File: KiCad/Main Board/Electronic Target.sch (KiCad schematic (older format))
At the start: 71 parts, among them J1 BHR-12-UVA, J10 EBWA-04-B, J11 640456-6, J12 0475890001, J9 Header 4x2, Q1 DWN1019UVT-7, Q2 DMN1019UVT-7, U1 PDSE1-S5-D6-M-TR, U2 LM339, U3 74HC74, U4 74LV8154, U5 74HC74, U6 74HC00, U7 74LV8154, U8 FT230XS-U, U9 LM75AIMX_NOPB, X1 8M0

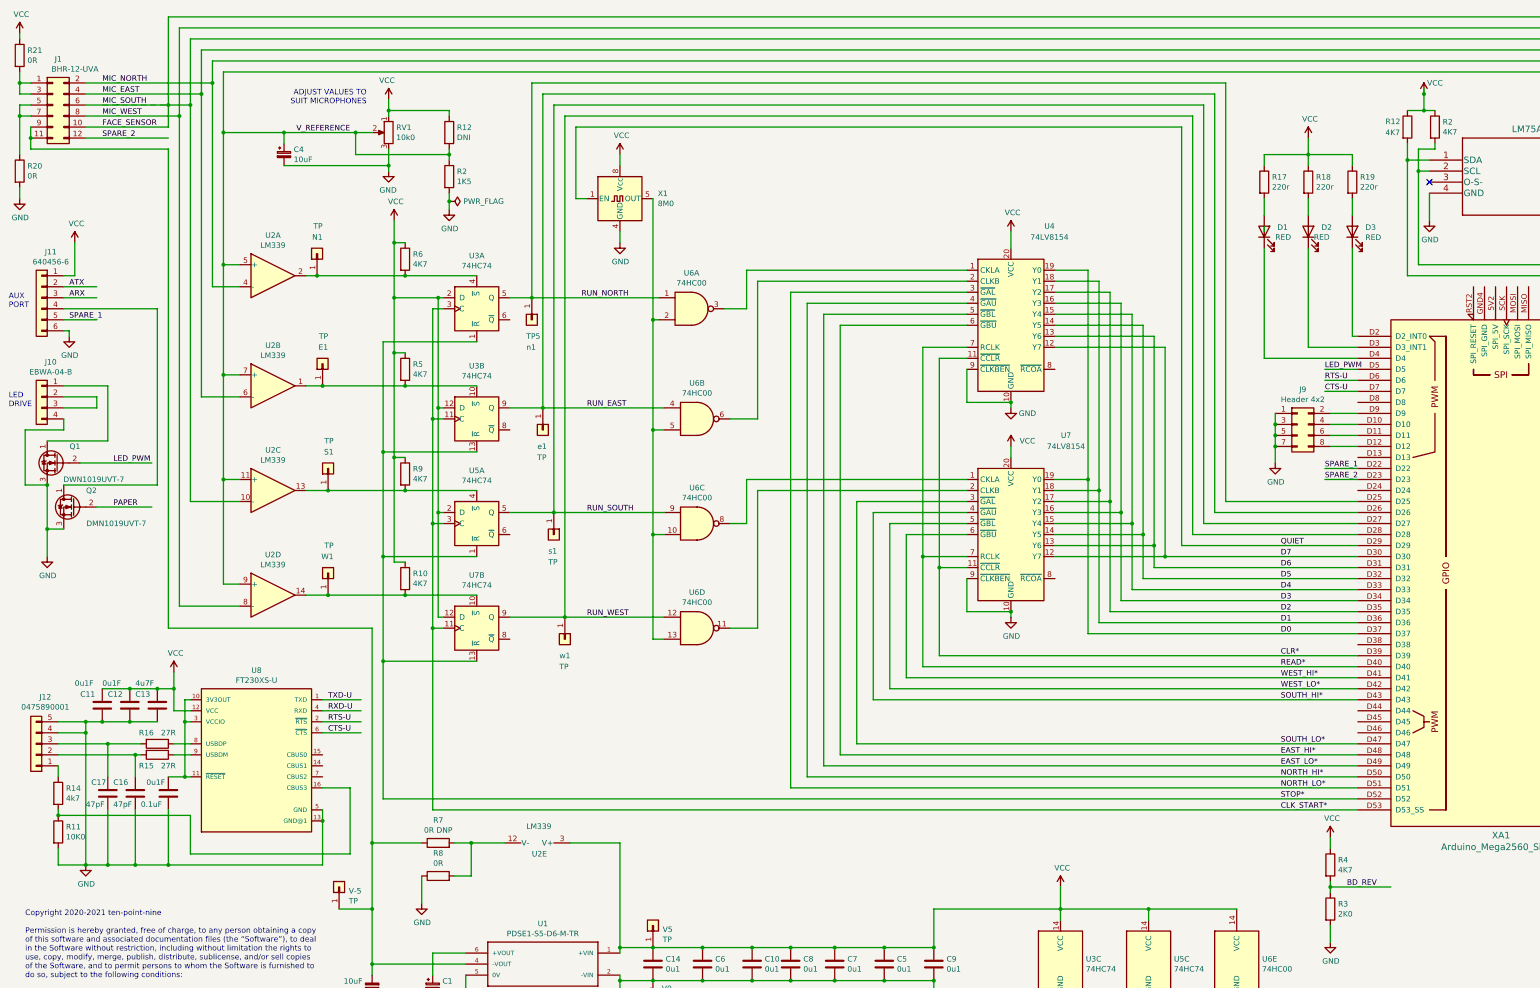
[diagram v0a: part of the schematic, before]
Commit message: Corrected errors in Schematic
Found a resistor error and reannotated the main board schematic
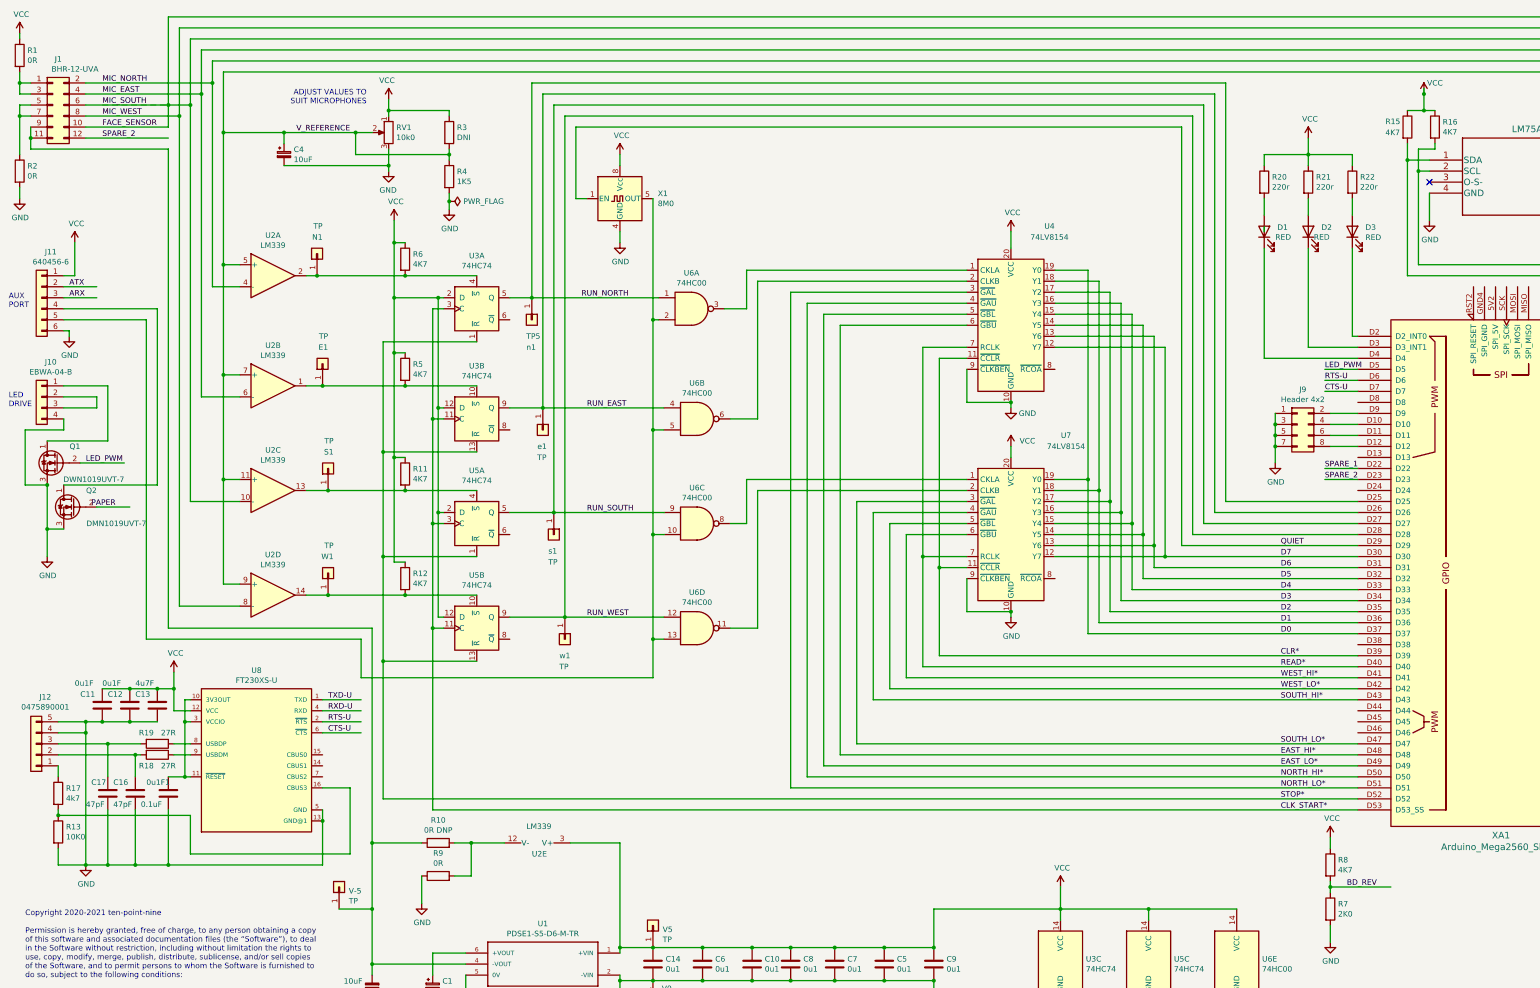
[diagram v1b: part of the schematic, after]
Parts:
- renumbered 0u1F to 0u1F1, R21 to R1, R7 to R10, R9 to R11, R10 to R12, R11 to R13, R12 to R15, R2 to R16, R14 to R17, R15 to R18, R16 to R19, R20 to R2, R17 to R20, R18 to R21, R19 to R22, R12 to R3, R2 to R4, R3 to R7, R4 to R8, R8 to R9, U7 to U5
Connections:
- wire segments 464 -> 469
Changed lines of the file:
@@
 $EndComp
 $Comp
-L 74xx:74HC74 U7
+L 74xx:74HC74 U5
 U 2 1 5E4CA7E2
 P 4750 6150
-F 0 "U7" H 4750 6631 50  0000 C CNN
+F 0 "U5" H 4750 6631 50  0000 C CNN
 F 1 "74HC74" H 4750 6540 50  0000 C CNN
 F 2 "Package_SO:SOIC-14_3.9x8.7mm_P1.27mm" H 4750 6150 50  0001 C CNN
@@
 $EndComp
 $Comp
-L Device:R R9
+L Device:R R11
 U 1 1 5E509479
 P 4100 4750
-F 0 "R9" H 4170 4796 50  0000 L CNN
+F 0 "R11" H 4170 4796 50  0000 L CNN
 F 1 "4K7" H 4170 4705 50  0000 L CNN
 F 2 "Resistor_SMD:R_0805_2012Metric" V 4030 4750 50  0001 C CNN
@@
 $EndComp
 $Comp
-L Device:R R10
+L Device:R R12
 U 1 1 5E50A682
 P 4100 5700
-F 0 "R10" H 4170 5746 50  0000 L CNN
+F 0 "R12" H 4170 5746 50  0000 L CNN
 F 1 "4K7" H 4170 5655 50  0000 L CNN
 F 2 "Resistor_SMD:R_0805_2012Metric" V 4030 5700 50  0001 C CNN
@@
 Connection ~ 2450 2850
 $Comp
-L Device:R R17
+L Device:R R20
 U 1 1 5E6769B9
 P 11900 2100
-F 0 "R17" H 11970 2146 50  0000 L CNN
+F 0 "R20" H 11970 2146 50  0000 L CNN
 F 1 "220r" H 11970 2055 50  0000 L CNN
 F 2 "Resistor_SMD:R_0805_2012Metric" V 11830 2100 50  0001 C CNN
@@
 $EndComp
 $Comp
-L Device:R R18
+L Device:R R21
 U 1 1 5E677C05
 P 12300 2100
-F 0 "R18" H 12370 2146 50  0000 L CNN
+F 0 "R21" H 12370 2146 50  0000 L CNN
 F 1 "220r" H 12370 2055 50  0000 L CNN
 F 2 "Resistor_SMD:R_0805_2012Metric" V 12230 2100 50  0001 C CNN
@@
 $EndComp
 $Comp
-L Device:R R19
+L Device:R R22
 U 1 1 5E6789DE
 P 12700 2100
-F 0 "R19" H 12770 2146 50  0000 L CNN
+F 0 "R22" H 12770 2146 50  0000 L CNN
 F 1 "220r" H 12770 2055 50  0000 L CNN
 F 2 "Resistor_SMD:R_0805_2012Metric" V 12630 2100 50  0001 C CNN
@@
 	2050 1500 2050 5950
 $Comp
-L Device:R R4
+L Device:R R8
 U 1 1 5F39A5E4
 P 12500 8300
-F 0 "R4" H 12570 8346 50  0000 L CNN
+F 0 "R8" H 12570 8346 50  0000 L CNN
 F 1 "4K7" H 12570 8255 50  0000 L CNN
 F 2 "Resistor_SMD:R_0805_2012Metric" V 12430 8300 50  0001 C CNN
@@
 $EndComp
 $Comp
-L Device:R R3
+L Device:R R7
 U 1 1 5F39B55C
 P 12500 8700
-F 0 "R3" H 12570 8746 50  0000 L CNN
+F 0 "R7" H 12570 8746 50  0000 L CNN
 F 1 "2K0" H 12570 8655 50  0000 L CNN
 F 2 "Resistor_SMD:R_0805_2012Metric" V 12430 8700 50  0001 C CNN
@@
 Connection ~ 13300 2000
 $Comp
-L Device:R R12
+L Device:R R15
 U 1 1 5ECCE730
 P 13200 1600
-F 0 "R12" H 13000 1650 50  0000 L CNN
+F 0 "R15" H 13000 1650 50  0000 L CNN
 F 1 "4K7" H 13000 1550 50  0000 L CNN
 F 2 "Resistor_SMD:R_0805_2012Metric" V 13130 1600 50  0001 C CNN
@@
 	3000 1650 3000 1750
 $Comp
-L Device:R R12
+L Device:R R3
 U 1 1 5EF502AF
 P 4500 1650
-F 0 "R12" H 4570 1696 50  0000 L CNN
+F 0 "R3" H 4570 1696 50  0000 L CNN
 F 1 "DNI" H 4570 1605 50  0000 L CNN
 F 2 "Resistor_SMD:R_0805_2012Metric" V 4430 1650 50  0001 C CNN
@@
 $EndComp
 $Comp
-L Device:R R2
+L Device:R R4
 U 1 1 5EF511BF
 P 4500 2050
-F 0 "R2" H 4570 2096 50  0000 L CNN
+F 0 "R4" H 4570 2096 50  0000 L CNN
 F 1 "1K5" H 4570 2005 50  0000 L CNN
 F 2 "Resistor_SMD:R_0805_2012Metric" V 4430 2050 50  0001 C CNN
@@
 	1200 7000 1200 7100
 $Comp
-L Device:R R16
+L Device:R R19
 U 1 1 6248BBEA
 P 1850 7200
-F 0 "R16" V 1750 7100 50  0000 C CNN
+F 0 "R19" V 1750 7100 50  0000 C CNN
 F 1 "27R" V 1750 7300 50  0000 C CNN
 F 2 "" V 1780 7200 50  0001 C CNN
@@
 Connection ~ 2100 7000
 $Comp
-L Device:C 0u1F
+L Device:C 0u1F1
 U 1 1 627F6E76
 P 1950 7650
-F 0 "0u1F" H 1750 7750 50  0000 L CNN
+F 0 "0u1F1" H 1750 7750 50  0000 L CNN
 F 1 "0.1uF" H 1700 7550 50  0000 L CNN
 F 2 "" H 1988 7500 50  0001 C CNN
@@
 Connection ~ 2000 6700
 $Comp
-L Device:R R14
+L Device:R R17
 U 1 1 628F8830
 P 950 7650
-F 0 "R14" H 1020 7696 50  0000 L CNN
+F 0 "R17" H 1020 7696 50  0000 L CNN
 F 1 "4k7" H 1020 7605 50  0000 L CNN
 F 2 "" V 880 7650 50  0001 C CNN
@@
 $EndComp
 $Comp
-L Device:R R11
+L Device:R R13
 U 1 1 628F9C9F
 P 950 8000
-F 0 "R11" H 1020 8046 50  0000 L CNN
+F 0 "R13" H 1020 8046 50  0000 L CNN
 F 1 "10K0" H 1020 7955 50  0000 L CNN
 F 2 "" V 880 8000 50  0001 C CNN
@@
 Wire Wire Line
 	1000 3450 1050 3450
-Text Label 1050 3350 0    50   ~ 0
-SPARE_1
 Wire Wire Line
 	12750 3800 12450 3800
@@
 	3800 8700 3800 9200
 $Comp
-L Device:R R7
+L Device:R R10
 U 1 1 632BC0C8
 P 4400 8100
-F 0 "R7" V 4607 8100 50  0000 C CNN
+F 0 "R10" V 4607 8100 50  0000 C CNN
 F 1 "0R DNP" V 4516 8100 50  0000 C CNN
 F 2 "" V 4330 8100 50  0001 C CNN
@@
 $EndComp
 $Comp
-L Device:R R8
+L Device:R R9
 U 1 1 632BD03A
 P 4400 8400
-F 0 "R8" V 4607 8400 50  0000 C CNN
+F 0 "R9" V 4607 8400 50  0000 C CNN
 F 1 "0R" V 4516 8400 50  0000 C CNN
 F 2 "" V 4330 8400 50  0001 C CNN
@@
 	1000 5250 850  5250
 Connection ~ 850  5250
-Wire Wire Line
-	1300 5050 1800 5050
-Wire Wire Line
-	1150 4650 1800 4650
-Text Label 1450 5050 0    50   ~ 0
+Text Label 1250 5050 0    50   ~ 0
 PAPER
-Text Label 1450 4650 0    50   ~ 0
+Text Label 1200 4650 0    50   ~ 0
 LED_PWM
 $Comp
@@
 	1000 4850 1850 4850
 $Comp
-L Device:R R15
+L Device:R R18
 U 1 1 6248CAE3
 P 1850 7300
-F 0 "R15" V 1950 7200 50  0000 C CNN
+F 0 "R18" V 1950 7200 50  0000 C CNN
 F 1 "27R" V 1950 7400 50  0000 C CNN
 F 2 "" V 1780 7300 50  0001 C CNN
@@
 	1050 3450 1050 3500
 Wire Wire Line
-	1000 3350 1300 3350
-Wire Wire Line
 	1000 4050 1300 4050
 Wire Wire Line
@@
 	3950 1450 4500 1450
 $Comp
-L Device:R R21
+L Device:R R1
 U 1 1 60854EF8
 P 600 950
-F 0 "R21" H 670 996 50  0000 L CNN
+F 0 "R1" H 670 996 50  0000 L CNN
 F 1 "0R" H 670 905 50  0000 L CNN
 F 2 "" V 530 950 50  0001 C CNN
@@
 Connection ~ 600  1200
 $Comp
-L Device:R R20
+L Device:R R2
 U 1 1 60A8F453
 P 600 2000
-F 0 "R20" H 670 2046 50  0000 L CNN
+F 0 "R2" H 670 2046 50  0000 L CNN
 F 1 "0R" H 670 1955 50  0000 L CNN
 F 2 "" V 530 2000 50  0001 C CNN
@@
 	4000 3150 4000 2650
 $Comp
-L Device:R R2
+L Device:R R16
 U 1 1 5ECCF75B
 P 13450 1600
-F 0 "R2" H 13520 1646 50  0000 L CNN
+F 0 "R16" H 13520 1646 50  0000 L CNN
 F 1 "4K7" H 13520 1555 50  0000 L CNN
 F 2 "Resistor_SMD:R_0805_2012Metric" V 13380 1600 50  0001 C CNN
@@
 Text Label 12050 7800 0    50   ~ 0
 CLK_START*
+Connection ~ 6350 6250
+Wire Wire Line
+	1150 4650 1550 4650
+Wire Wire Line
+	1300 5050 1600 5050
+Wire Wire Line
+	1000 3350 1750 3350
+Wire Wire Line
+	1750 3350 1750 6250
+Wire Wire Line
+	1750 6250 3700 6250
+Wire Wire Line
+	3700 6250 3700 6600
+Wire Wire Line
+	3700 6600 6350 6600
+Wire Wire Line
+	6350 6250 6350 6600
 $EndSCHEMATC
